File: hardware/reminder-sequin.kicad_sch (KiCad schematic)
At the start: 47 parts, among them J1 USB_C_Receptacle_USB2.0_16P, SW1 User, SW2 RST, SW3 BOOTSEL, U1 RP2040, U3 FM24C64B, U4 W25Q32JVSS, Y1 12MHz

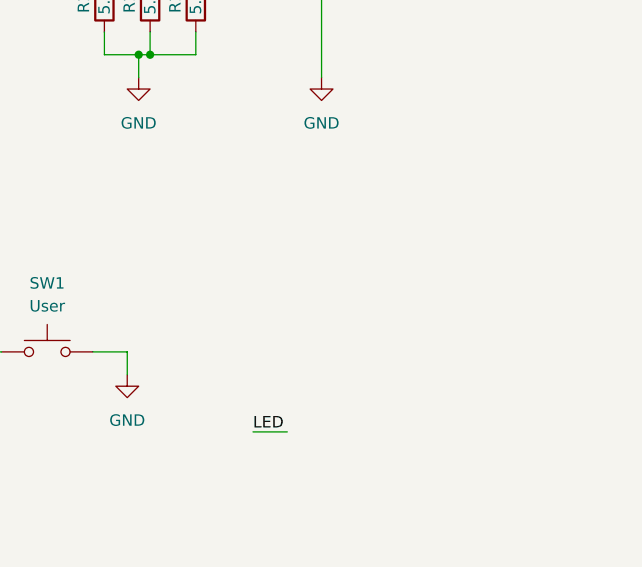
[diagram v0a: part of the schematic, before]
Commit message: mounting holes
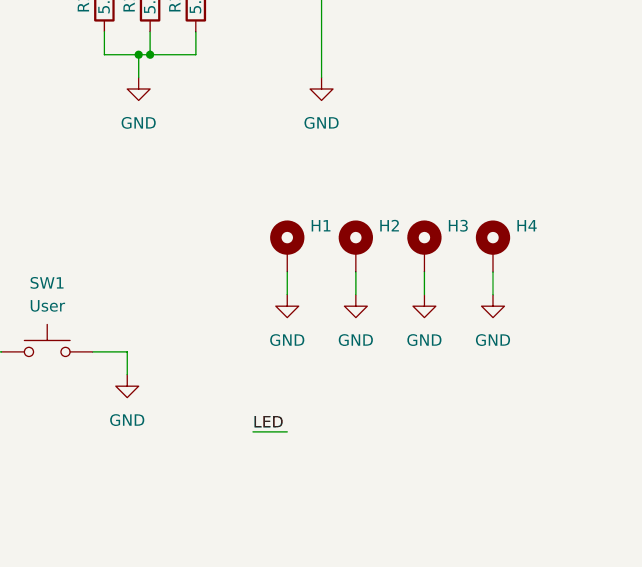
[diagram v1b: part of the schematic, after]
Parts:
- added H1, H2, H3, H4: MountingHole_Pad, MountingHole:MountingHole_2.2mm_M2_ISO7380_Pad, symbol Mechanical:MountingHole_Pad
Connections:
- net GND: now also H1.1, H2.1, H3.1, H4.1

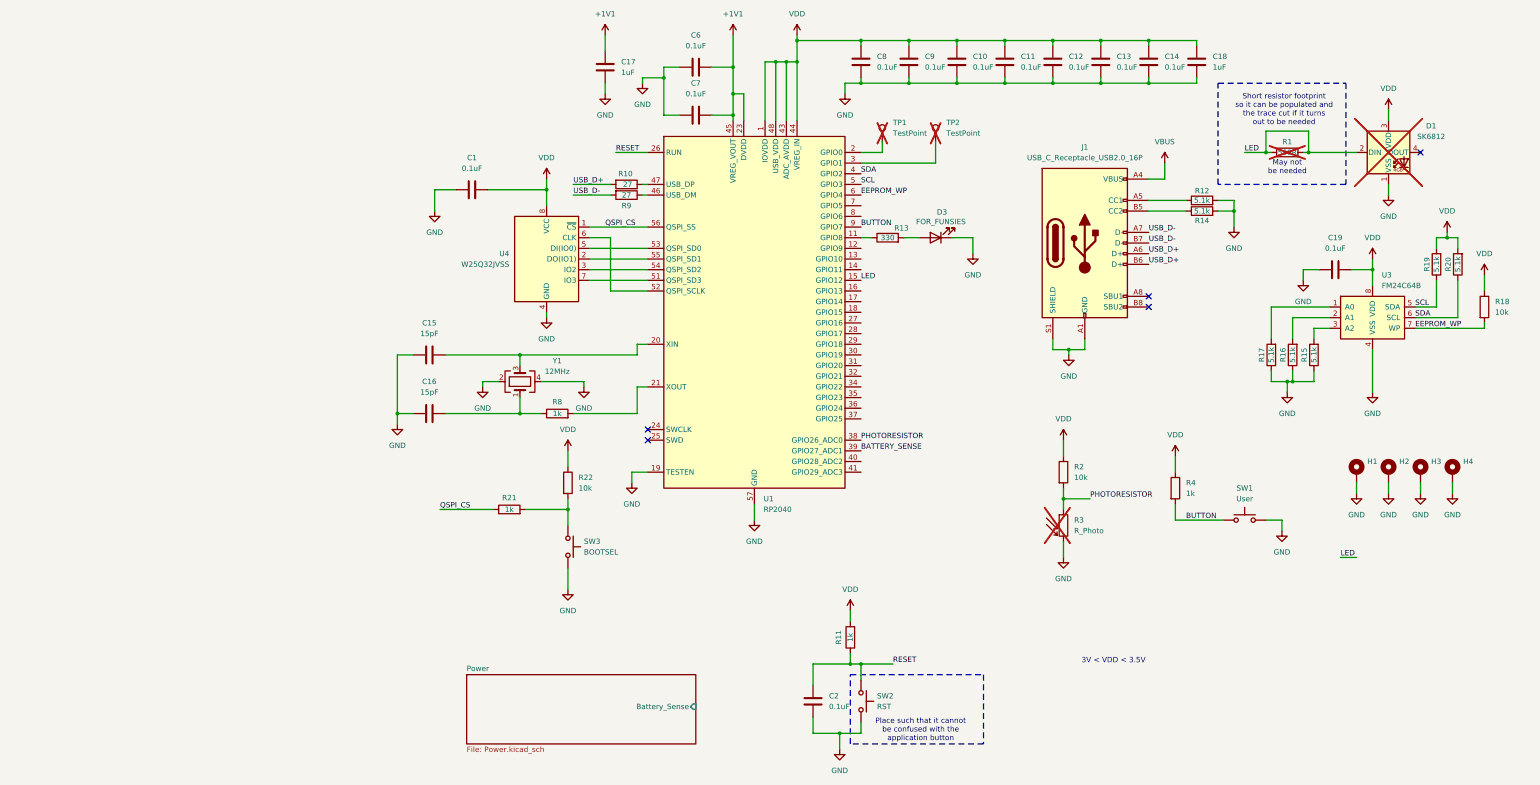
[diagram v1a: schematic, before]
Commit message: redid design based on STM3201
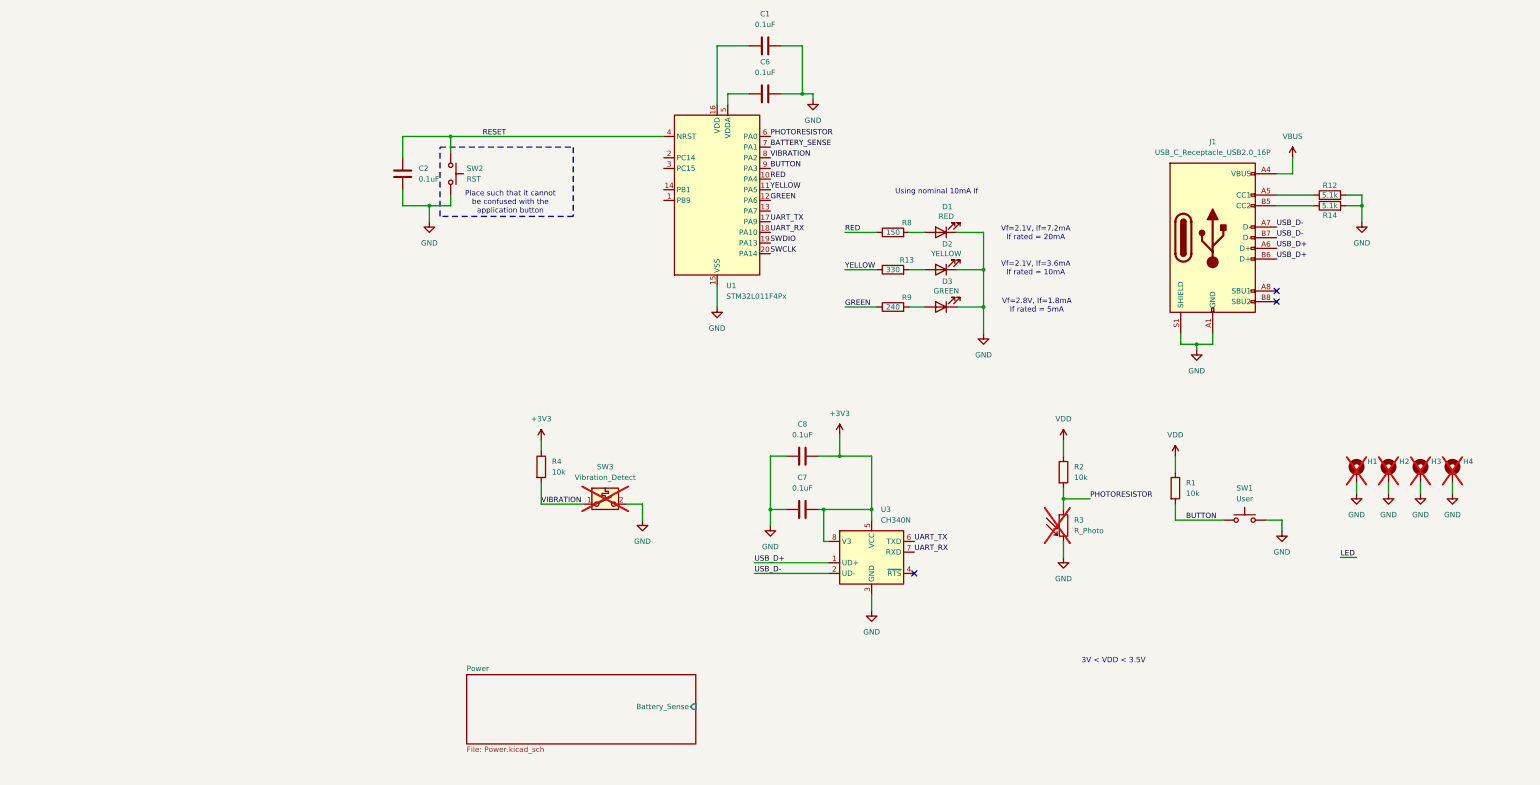
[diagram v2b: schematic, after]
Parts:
- removed C10, C11, C12, C13, C14, C19, C9: 0.1uF, Capacitor_SMD:C_0402_1005Metric, symbol Device:C
- removed C15, C16: 15pF, Capacitor_SMD:C_0402_1005Metric, symbol Device:C
- removed C17, C18: 1uF, Capacitor_SMD:C_0805_2012Metric, symbol Device:C
- removed D1: SK6812, LED_SMD:LED_SK6812_PLCC4_5.0x5.0mm_P3.2mm, symbol LED:SK6812
- removed R10: 27, Resistor_SMD:R_0603_1608Metric, symbol Device:R
- removed R11, R21: 1k, Resistor_SMD:R_0402_1005Metric, symbol Device:R
- removed R15, R16, R17, R19, R20: 5.1k, Resistor_SMD:R_0402_1005Metric, symbol Device:R
- removed R18, R22: 10k, Resistor_SMD:R_0402_1005Metric, symbol Device:R
- removed SW3: BOOTSEL, cat:TS-1088-AR02016, symbol Switch:SW_Push
- removed TP1, TP2: TestPoint, TestPoint:TestPoint_Pad_3.0x3.0mm, symbol Connector:TestPoint
- removed U1: RP2040, Package_DFN_QFN:QFN-56-1EP_7x7mm_P0.4mm_EP3.2x3.2mm, symbol MCU_RaspberryPi:RP2040
- removed U3: FM24C64B, Package_SO:SOIC-8_3.9x4.9mm_P1.27mm, symbol Memory_NVRAM:FM24C64B
- removed U4: W25Q32JVSS, Package_SO:SOIC-8_5.23x5.23mm_P1.27mm, symbol Memory_Flash:W25Q32JVSS
- removed Y1: 12MHz, Crystal:Crystal_SMD_Abracon_ABM8G-4Pin_3.2x2.5mm, symbol Device:Crystal_GND24
- added D1: RED, LED_SMD:LED_0603_1608Metric, symbol Device:LED
- added D3: GREEN, LED_SMD:LED_0805_2012Metric, symbol Device:LED
- added SW3: Vibration_Detect, symbol Switch:SW_SPST_Temperature
- added U1: STM32L011F4Px, Package_SO:TSSOP-20_4.4x6.5mm_P0.65mm, symbol MCU_ST_STM32L0:STM32L011F4Px
- added U3: CH340N, Package_SO:SOP-8_3.9x4.9mm_P1.27mm, symbol Interface_USB:CH340N
- D2: renamed from D3; value FOR_FUNSIES -> YELLOW
- H1, H2, H3, H4: now not fitted
- R1: value 500R -> 10k; footprint Resistor_SMD:R_0603_1608Metric -> Resistor_SMD:R_0402_1005Metric; LCSC Part # (none) -> C25744; now fitted
- R4: value 1k -> 10k; LCSC Part # C11702 -> C25744
- R8: value 1k -> 150; LCSC Part # C11702 -> C25082
- R9: value 27 -> 240; LCSC Part # C25190 -> C23350
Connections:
- net +1V1 is gone; now on net GND: C6.2, C7.2
- net BATTERY_SENSE: now also U1.7 (PA1)
- net BUTTON: now also R1.2, U1.9 (PA3); no longer R4.2
- net GND: now also C1.2, C8.2, D1.1 (K), D3.1 (K), SW3.2 (B), U1.15 (VSS), U3.3 (GND); no longer C1.1, C6.1, C7.1, C8.1
- net LED: no longer R1.1, R1.2
- net PHOTORESISTOR: now also U1.6 (PA0)
- net RESET: now also U1.4 (NRST)
- net USB_D+: now also U3.1 (UD+)
- net USB_D-: now also U3.2 (UD-); no longer R9.2
- net VDD: now also R1.1; no longer C1.2, C8.2, R4.1
- net RED: now reaches R8.1
- net RED: now also U1.10 (PA4)
- net at R8.2: now also D1.2 (A)
- net YELLOW: now reaches R13.1
- net YELLOW: now also U1.11 (PA5)
- net GREEN: now reaches R9.1
- net GREEN: now also U1.12 (PA6)
- new net: C6.1, U1.5 (VDDA)
- new net: C1.1, U1.16 (VDD)
- new net: D3.2 (A), R9.2
- new net +3V3: C7.1, C8.1, R4.1, U3.5 (VCC), U3.8 (V3)
- new net SWCLK: U1.20 (PA14)
- new net SWDIO: U1.19 (PA13)
- new net UART_RX: U1.18 (PA10), U3.7 (RXD)
- new net UART_TX: U1.17 (PA9), U3.6 (TXD)
- new net VIBRATION: R4.2, SW3.1 (A), U1.8 (PA2)
- no-connect marks 5 -> 3
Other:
- note added: "Using nominal 10mA If"
- note added: "Vf=2.1V, If=3.6mA If rated = 10mA"
- note added: "Vf=2.1V, If=7.2mA If rated = 20mA"
- note added: "Vf=2.8V, If=1.8mA If rated = 5mA"
- note removed: "May not be needed"
- note removed: "Short resistor footprint so it can be populated and the trace cut if it turns out to be needed"
- moved on the sheet: C2, D2, J1, R12, R13, R14, SW2

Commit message: design polishing
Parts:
- added C10, C9: 10pF, Capacitor_SMD:C_0402_1005Metric, symbol Device:C
- added Y1: 32.768kHz, Crystal:Crystal_SMD_3215-2Pin_3.2x1.5mm, symbol Device:Crystal
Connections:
- net GND: now also C10.2, C9.2
- net at U1.2 (PC14): now also C9.1, Y1.2
- net at U1.3 (PC15): now also C10.1, Y1.1
- no-connect marks 3 -> 6
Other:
- note added: "Place such that reset button cannot be confused with the application button"
- note removed: "Place such that it cannot be confused with the application button"

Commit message: stuff
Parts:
- added J2: uart, Connector_PinHeader_2.54mm:PinHeader_1x06_P2.54mm_Vertical, symbol Connector_Generic:Conn_01x06
- added J3: swd, Connector_PinHeader_2.54mm:PinHeader_1x06_P2.54mm_Vertical, symbol Connector_Generic:Conn_01x06
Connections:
- net +3V3: now also J3.1 (Pin_1)
- net GND: now also J2.1 (Pin_1), J3.3 (Pin_3)
- net RESET: now also J3.5 (Pin_5)
- net SWCLK: now also J3.2 (Pin_2)
- net SWDIO: now also J3.4 (Pin_4)
- net UART_RX: now also J2.5 (Pin_5)
- net UART_TX: now also J2.4 (Pin_4)
- no-connect marks 6 -> 10
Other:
- note added: "Need to figure out how to use this for power when plugged in"

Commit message: started layout
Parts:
- R3: footprint Connector_JST:JST_XH_B2B-XH-AM_1x02_P2.50mm_Vertical -> LED_THT:LED_D5.0mm_FlatTop
- SW3: footprint (none) -> Capacitor_THT:CP_Radial_D5.0mm_P2.00mm
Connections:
- net +3V3: now also C1.1, C6.1, U1.16 (VDD), U1.5 (VDDA)
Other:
- note removed: "Need to figure out how to use this for power when plugged in"
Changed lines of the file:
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@@
 	)
 	(junction
+		(at 92.71 27.94)
+		(diameter 0)
+		(color 0 0 0 0)
+	)
+	(junction
 		(at 207.01 92.71)
 		(diameter 0)
@@
 	)
 	(junction
+		(at 92.71 21.59)
+		(diameter 0)
+		(color 0 0 0 0)
+	)
+	(junction
 		(at 113.03 33.02)
 		(diameter 0)
@@
 	)
 	(junction
+		(at 95.25 33.02)
+		(diameter 0)
+		(color 0 0 0 0)
+	)
+	(junction
 		(at 69.85 54.61)
 		(diameter 0)
@@
 	(wire
 		(pts
+			(xy 95.25 27.94) (xy 92.71 27.94)
+		)
+		(stroke
+			(width 0)
+			(type default)
+		)
+	)
+	(wire
+		(pts
 			(xy 158.75 21.59) (xy 153.67 21.59)
 		)
@@
 	(wire
 		(pts
+			(xy 95.25 33.02) (xy 95.25 27.94)
+		)
+		(stroke
+			(width 0)
+			(type default)
+		)
+	)
+	(wire
+		(pts
 			(xy 17.78 55.88) (xy 17.78 59.69)
 		)
@@
 	(wire
 		(pts
+			(xy 92.71 19.05) (xy 92.71 21.59)
+		)
+		(stroke
+			(width 0)
+			(type default)
+		)
+	)
+	(wire
+		(pts
 			(xy 124.46 21.59) (xy 124.46 22.86)
 		)
@@
 	(wire
 		(pts
-			(xy 92.71 21.59) (xy 92.71 35.56)
+			(xy 92.71 21.59) (xy 92.71 27.94)
 		)
 		(stroke
@@
 	(wire
 		(pts
+			(xy 92.71 27.94) (xy 92.71 35.56)
+		)
+		(stroke
+			(width 0)
+			(type default)
+		)
+	)
+	(wire
+		(pts
 			(xy 95.25 35.56) (xy 95.25 33.02)
 		)
@@
 		)
 	)
-	(text "Need to figure out how to use\nthis for power when plugged in"
-		(exclude_from_sim no)
-		(at 260.35 77.47 0)
-		(effects
-			(font
-				(size 1.27 1.27)
-			)
-		)
-	)
 	(text "Vf=2.1V, If=7.2mA\nIf rated = 20mA"
 		(exclude_from_sim no)
@@
 		)
 	)
+	(label "BATTERY_SENSE"
+		(at 87.63 179.07 0)
+		(effects
+			(font
+				(size 1.27 1.27)
+			)
+			(justify left bottom)
+		)
+	)
 	(label "UART_TX"
 		(at 134.62 29.21 180)
@@
 	)
 	(symbol
+		(lib_id "power:+3V3")
+		(at 92.71 19.05 0)
+		(unit 1)
+		(exclude_from_sim no)
+		(in_bom yes)
+		(on_board yes)
+		(dnp no)
+		(fields_autoplaced yes)
+		(property "Reference" "#PWR34"
+			(at 92.71 22.86 0)
+			(effects
+				(font
+					(size 1.27 1.27)
+				)
+				(hide yes)
+			)
+		)
+		(property "Value" "+3V3"
+			(at 92.71 13.97 0)
+			(effects
+				(font
+					(size 1.27 1.27)
+				)
+			)
+		)
+		(property "Footprint" ""
+			(at 92.71 19.05 0)
+			(effects
+				(font
+					(size 1.27 1.27)
+				)
+				(hide yes)
+			)
+		)
+		(property "Datasheet" ""
+			(at 92.71 19.05 0)
+			(effects
+				(font
+					(size 1.27 1.27)
+				)
+				(hide yes)
+			)
+		)
+		(property "Description" "Power symbol creates a global label with name \"+3V3\""
+			(at 92.71 19.05 0)
+			(effects
+				(font
+					(size 1.27 1.27)
+				)
+				(hide yes)
+			)
+		)
+		(pin "1"
+		)
+		(instances
+			(project ""
+				(path "/3313c311-f70a-45a8-bbf4-c9e4cbd18d5c"
+					(reference "#PWR34")
+					(unit 1)
+				)
+			)
+		)
+	)
+	(symbol
 		(lib_id "MCU_ST_STM32L0:STM32L011F4Px")
 		(at 92.71 58.42 0)
@@
 			)
 		)
-		(property "Footprint" "Connector_JST:JST_XH_B2B-XH-AM_1x02_P2.50mm_Vertical"
+		(property "Footprint" "LED_THT:LED_D5.0mm_FlatTop"
 			(at 176.53 142.24 90)
 			(effects
@@
 			)
 		)
-		(property "Footprint" ""
+		(property "Footprint" "Capacitor_THT:CP_Radial_D5.0mm_P2.00mm"
 			(at 66.04 130.81 0)
 			(effects

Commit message: bom improvements
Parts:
- removed R4: 10k, Resistor_SMD:R_0402_1005Metric, symbol Device:R
- added R11: 5.1k, Resistor_SMD:R_0402_1005Metric, symbol Device:R
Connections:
- net +3V3: now also SW3.2 (B)
- net BATTERY_SENSE: now also U1.9 (PA3); no longer U1.7 (PA1)
- net BUTTON: now also U1.12 (PA6); no longer U1.9 (PA3)
- net GND: now also R11.2; no longer SW3.2 (B)
- net GREEN: now also U1.8 (PA2); no longer U1.12 (PA6)
- net PHOTORESISTOR: now also U1.10 (PA4); no longer U1.6 (PA0)
- net RED: now also U1.11 (PA5); no longer U1.10 (PA4)
- net VIBRATION: now also U1.6 (PA0), R11.1; no longer U1.8 (PA2)
- net YELLOW: now also U1.7 (PA1); no longer U1.11 (PA5)
- net VDD renamed 3V3
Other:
- note added: "3V < 3V3 < 3.5V"
- note removed: "3V < VDD < 3.5V"
- moved on the sheet: SW3
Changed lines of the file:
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@@
 	(wire
 		(pts
-			(xy 71.12 130.81) (xy 74.93 130.81)
-		)
-		(stroke
-			(width 0)
-			(type default)
-		)
-	)
-	(wire
-		(pts
 			(xy 74.93 130.81) (xy 74.93 134.62)
 		)
@@
 	(wire
 		(pts
-			(xy 50.8 130.81) (xy 60.96 130.81)
+			(xy 50.8 130.81) (xy 62.23 130.81)
 		)
 		(stroke
@@
 	(wire
 		(pts
-			(xy 50.8 115.57) (xy 50.8 118.11)
+			(xy 50.8 113.03) (xy 50.8 115.57)
+		)
+		(stroke
+			(width 0)
+			(type default)
+		)
+	)
+	(wire
+		(pts
+			(xy 69.85 130.81) (xy 74.93 130.81)
 		)
 		(stroke
@@
 		)
 	)
-	(text "3V < VDD < 3.5V"
+	(text "3V < 3V3 < 3.5V"
 		(exclude_from_sim no)
 		(at 187.198 168.148 0)
@@
 	)
 	(label "PHOTORESISTOR"
-		(at 105.41 43.18 0)
+		(at 105.41 53.34 0)
 		(effects
 			(font
@@
 	)
 	(label "BUTTON"
-		(at 105.41 50.8 0)
+		(at 105.41 58.42 0)
 		(effects
 			(font
@@
 	)
 	(label "BATTERY_SENSE"
-		(at 105.41 45.72 0)
+		(at 105.41 50.8 0)
 		(effects
 			(font
@@
 	)
 	(label "YELLOW"
-		(at 105.41 55.88 0)
+		(at 105.41 45.72 0)
 		(effects
 			(font
@@
 	)
 	(label "RED"
-		(at 105.41 53.34 0)
+		(at 105.41 55.88 0)
 		(effects
 			(font
@@
 	)
 	(label "GREEN"
-		(at 105.41 58.42 0)
+		(at 105.41 48.26 0)
 		(effects
 			(font
@@
 	)
 	(label "VIBRATION"
-		(at 105.41 48.26 0)
+		(at 105.41 43.18 0)
 		(effects
 			(font
@@
 	)
 	(symbol
+		(lib_id "Device:R")
+		(at 66.04 130.81 90)
+		(unit 1)
+		(exclude_from_sim no)
+		(in_bom yes)
+		(on_board yes)
+		(dnp no)
+		(property "Reference" "R11"
+			(at 66.04 133.096 90)
+			(effects
+				(font
+					(size 1.27 1.27)
+				)
+			)
+		)
+		(property "Value" "5.1k"
+			(at 66.04 130.81 90)
+			(effects
+				(font
+					(size 1.27 1.27)
+				)
+			)
+		)
+		(property "Footprint" "Resistor_SMD:R_0402_1005Metric"
+			(at 66.04 132.588 90)
+			(effects
+				(font
+					(size 1.27 1.27)
+				)
+				(hide yes)
+			)
+		)
+		(property "Datasheet" "~"
+			(at 66.04 130.81 0)
+			(effects
+				(font
+					(size 1.27 1.27)
+				)
+				(hide yes)
+			)
+		)
+		(property "Description" "Resistor"
+			(at 66.04 130.81 0)
+			(effects
+				(font
+					(size 1.27 1.27)
+				)
+				(hide yes)
+			)
+		)
+		(property "LCSC Part #" "C25905"
+			(at 66.04 130.81 0)
+			(effects
+				(font
+					(size 1.27 1.27)
+				)
+				(hide yes)
+			)
+		)
+		(pin "2"
+		)
+		(pin "1"
+		)
+		(instances
+			(project "reminder-sequin"
+				(path "/3313c311-f70a-45a8-bbf4-c9e4cbd18d5c"
+					(reference "R11")
+					(unit 1)
+				)
+			)
+		)
+	)
+	(symbol
 		(lib_id "Connector_Generic:Conn_01x06")
 		(at 139.7 26.67 0)
@@
 	(symbol
 		(lib_id "power:+3V3")
-		(at 50.8 115.57 0)
+		(at 50.8 113.03 0)
 		(unit 1)
 		(exclude_from_sim no)
@@
 		(fields_autoplaced yes)
 		(property "Reference" "#PWR19"
-			(at 50.8 119.38 0)
+			(at 50.8 116.84 0)
 			(effects
 				(font
@@
 		)
 		(property "Value" "+3V3"
-			(at 50.8 110.49 0)
+			(at 50.8 107.95 0)
 			(effects
 				(font
@@
 		)
 		(property "Footprint" ""
-			(at 50.8 115.57 0)
+			(at 50.8 113.03 0)
 			(effects
 				(font
@@
 		)
 		(property "Datasheet" ""
-			(at 50.8 115.57 0)
+			(at 50.8 113.03 0)
 			(effects
 				(font
@@
 		)
 		(property "Description" "Power symbol creates a global label with name \"+3V3\""
-			(at 50.8 115.57 0)
+			(at 50.8 113.03 0)
 			(effects
 				(font
@@
 	)
 	(symbol
-		(lib_id "Device:R")
-		(at 50.8 121.92 0)
-		(unit 1)
-		(exclude_from_sim no)
-		(in_bom yes)
-		(on_board yes)
-		(dnp no)
-		(fields_autoplaced yes)
-		(property "Reference" "R4"
-			(at 53.34 120.6499 0)
-			(effects
-				(font
-					(size 1.27 1.27)
-				)
-				(justify left)
-			)
-		)
-		(property "Value" "10k"
-			(at 53.34 123.1899 0)
-			(effects
-				(font
-					(size 1.27 1.27)
-				)
-				(justify left)
-			)
-		)
-		(property "Footprint" "Resistor_SMD:R_0402_1005Metric"
-			(at 49.022 121.92 90)
-			(effects
-				(font
-					(size 1.27 1.27)
-				)
-				(hide yes)
-			)
-		)
-		(property "Datasheet" "~"
-			(at 50.8 121.92 0)
-			(effects
-				(font
-					(size 1.27 1.27)
-				)
-				(hide yes)
-			)
-		)
-		(property "Description" "Resistor"
-			(at 50.8 121.92 0)
-			(effects
-				(font
-					(size 1.27 1.27)
-				)
-				(hide yes)
-			)
-		)
-		(property "Cost" ""
-			(at 50.8 121.92 0)
-			(effects
-				(font
-					(size 1.27 1.27)
-				)
-				(hide yes)
-			)
-		)
-		(property "LCSC Part #" " C25744"
-			(at 50.8 121.92 0)
-			(effects
-				(font
-					(size 1.27 1.27)
-				)
-				(hide yes)
-			)
-		)
-		(pin "1"
-		)
-		(pin "2"
-		)
-		(instances
-			(project "reminder-sequin"
-				(path "/3313c311-f70a-45a8-bbf4-c9e4cbd18d5c"
-					(reference "R4")
-					(unit 1)
-				)
-			)
-		)
-	)
-	(symbol
 		(lib_id "Switch:SW_SPST_Temperature")
-		(at 66.04 130.81 0)
+		(at 50.8 120.65 90)
 		(unit 1)
 		(exclude_from_sim no)
@@
 		(fields_autoplaced yes)
 		(property "Reference" "SW3"
-			(at 66.04 121.92 0)
+			(at 53.34 119.3799 90)
 			(effects
 				(font
 					(size 1.27 1.27)
 				)
+				(justify right)
 			)
 		)
 		(property "Value" "Vibration_Detect"
-			(at 66.04 124.46 0)
+			(at 53.34 121.9199 90)
 			(effects
 				(font
 					(size 1.27 1.27)
 				)
+				(justify right)
 			)
 		)
 		(property "Footprint" "Capacitor_THT:CP_Radial_D5.0mm_P2.00mm"
-			(at 66.04 130.81 0)
+			(at 50.8 120.65 0)
 			(effects
 				(font
@@
 		)
 		(property "Datasheet" "~"
-			(at 66.04 135.89 0)
+			(at 55.88 120.65 0)
 			(effects
 				(font
@@
 		)
 		(property "Description" "Single Pole Single Throw (SPST) switch, temperature dependent"
-			(at 66.04 130.81 0)
+			(at 50.8 120.65 0)
 			(effects
 				(font
@@
 		(on_board yes)
 		(dnp no)
-		(fields_autoplaced yes)
 		(property "Reference" "#PWR2"
 			(at 115.57 40.64 0)
@@
 		)
 		(property "Value" "GND"
-			(at 115.57 39.37 0)
+			(at 130.81 44.45 0)
 			(effects
 				(font
@@
 			)
 		)
-		(property "Value" "VDD"
+		(property "Value" "3V3"
 			(at 201.93 114.3 0)
 			(effects
@@
 			)
 		)
-		(property "Value" "VDD"
+		(property "Value" "3V3"
 			(at 175.26 110.49 0)
 			(effects

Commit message: bom improvements
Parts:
- added U6: CP2102, Package_DFN_QFN:QFN-28-1EP_5x5mm_P0.5mm_EP3.35x3.35mm, symbol cat:CP2102
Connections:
- new net: U6.29 (GND), U6.3 (GND)
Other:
- moved on the sheet: C7, C8, U3
